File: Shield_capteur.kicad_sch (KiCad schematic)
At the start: 4 parts, among them J1 Power, J2 Digital/PWM, J3 Analog, J4 Digital/PWM

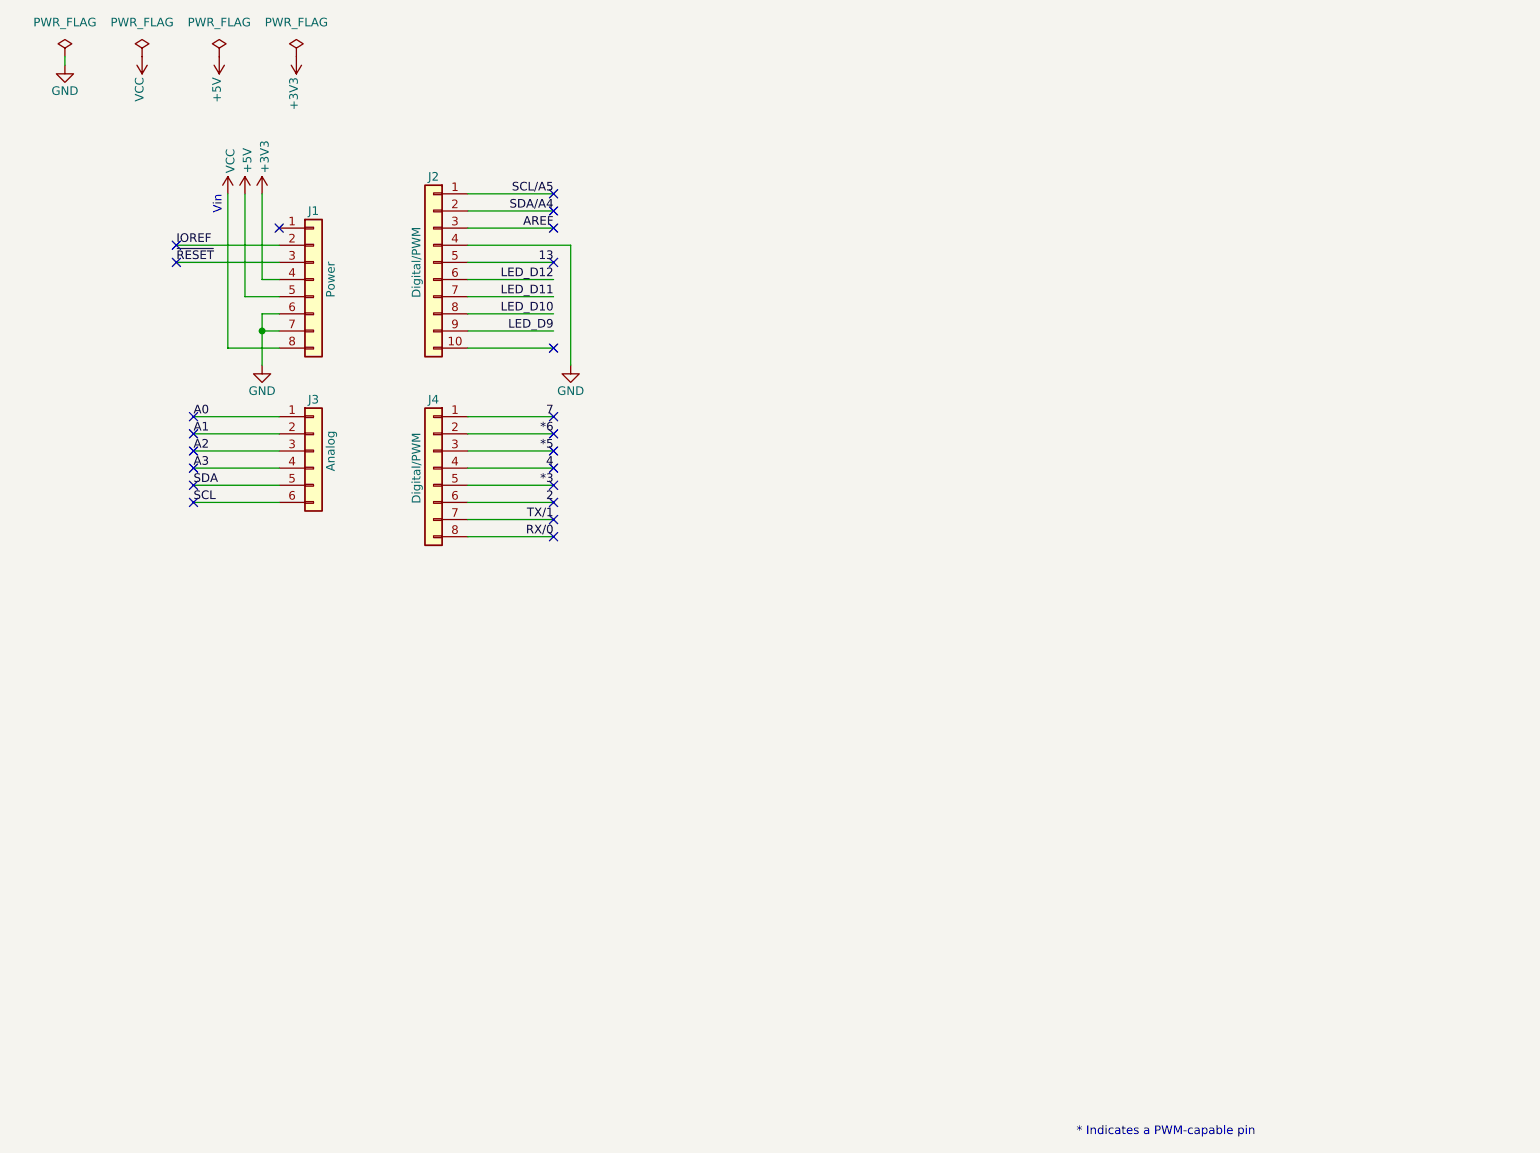
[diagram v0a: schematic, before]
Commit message: Avancée sur le shield, schéma +footprint
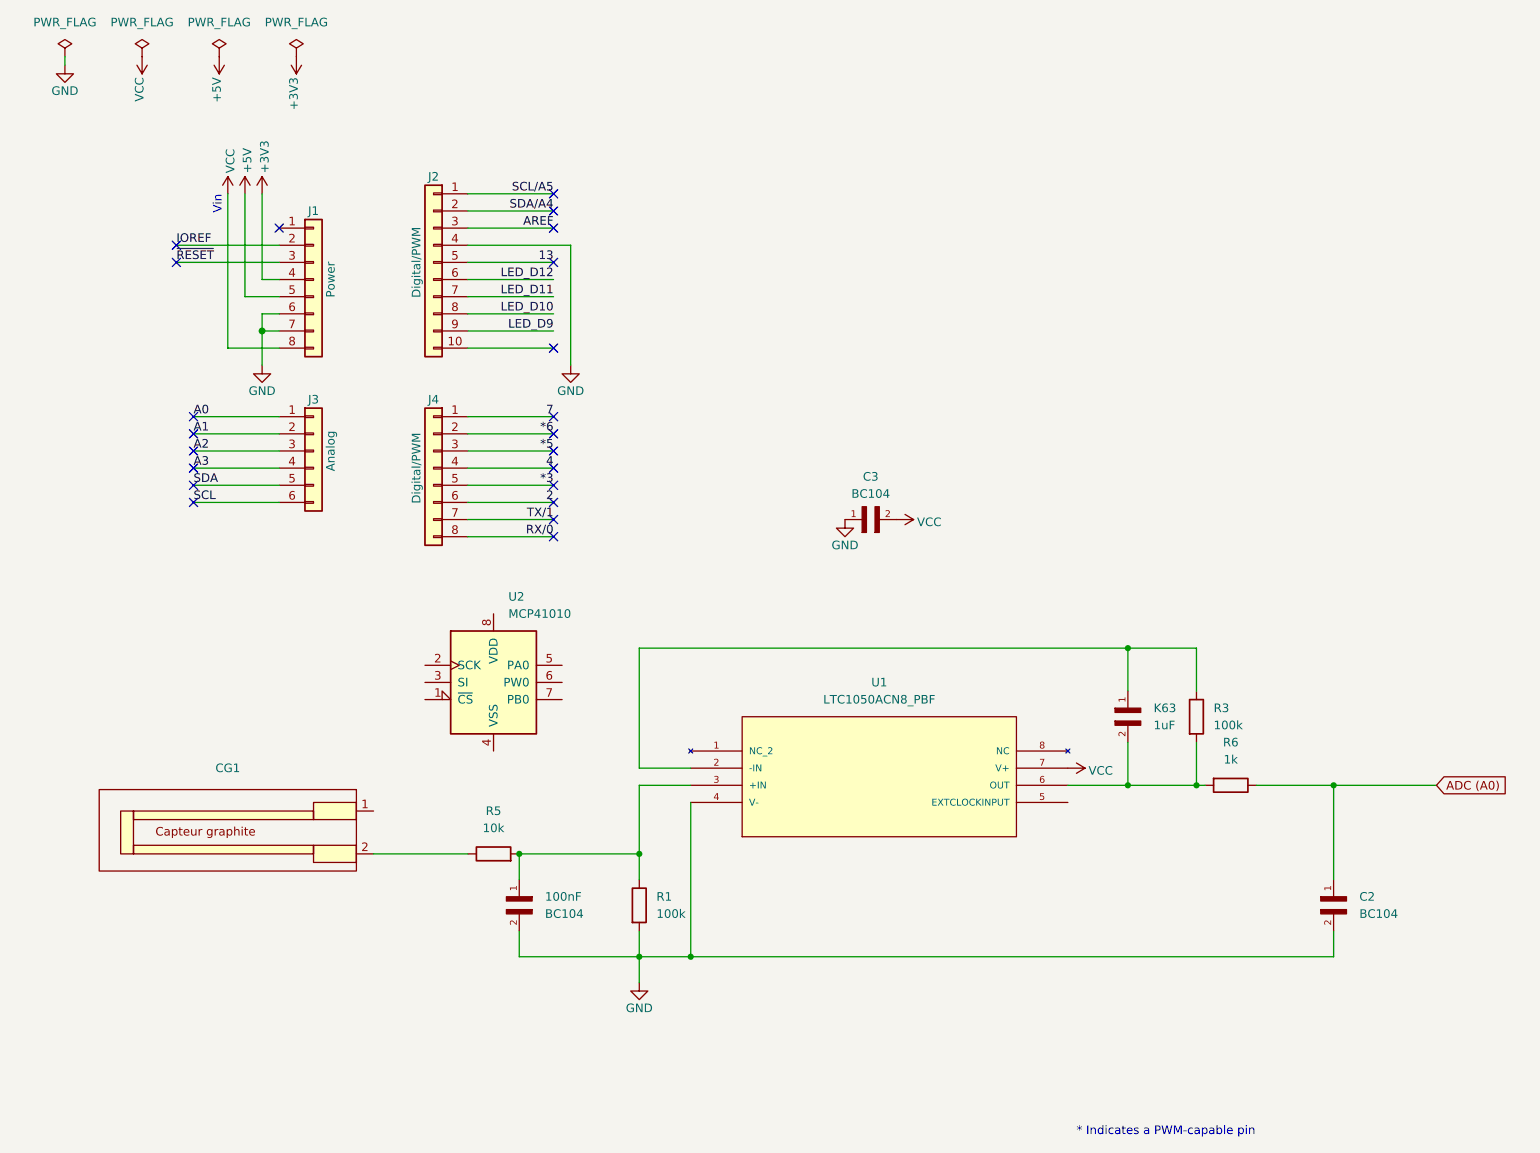
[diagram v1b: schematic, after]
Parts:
- added BC104: 100nF, Capacitor_THT:C_Disc_D5.0mm_W2.5mm_P5.00mm, symbol GRM033B31A104KE84D:GRM033B31A104KE84D
- added C2, C3: BC104, Capacitor_THT:C_Disc_D5.0mm_W2.5mm_P5.00mm, symbol GRM033B31A104KE84D:GRM033B31A104KE84D
- added CG1: ~, Connector_PinSocket_2.54mm:PinSocket_1x02_P2.54mm_Vertical, symbol New_Library_symbol_capteur:Capteur_graphite
- added K63: 1uF, Capacitor_THT:C_Rect_L7.0mm_W4.5mm_P5.00mm, symbol GRM033B31A104KE84D:GRM033B31A104KE84D
- added R1, R3: 100k, Resistor_THT:R_Axial_DIN0207_L6.3mm_D2.5mm_P10.16mm_Horizontal, symbol Device:R
- added R5: 10k, Resistor_THT:R_Axial_DIN0207_L6.3mm_D2.5mm_P10.16mm_Horizontal, symbol Device:R
- added R6: 1k, Resistor_THT:R_Axial_DIN0207_L6.3mm_D2.5mm_P10.16mm_Horizontal, symbol Device:R
- added U1: LTC1050ACN8_PBF, LTC1050ACN8_PBF:PDIP-8_N, symbol LTC1050ACN8_PBF:LTC1050ACN8_PBF
- added U2: MCP41010, symbol Potentiometer_Digital:MCP41010
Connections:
- net GND: now also BC104.2, C2.2, C3.1, R1.2, U1.4 (V-)
- net VCC: now also C3.2, U1.7 (V+)
- new net: BC104.1, R1.1, R5.2, U1.3 (+IN)
- new net: K63.2, R3.2, R6.2, U1.6 (OUT)
- new net: K63.1, R3.1, U1.2 (-IN)
- new net: CG1.2, R5.1
- new net ADC (A0): C2.1, R6.1

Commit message: Progrès TD Datasheet
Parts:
- added HC-1: ~, Connector_PinSocket_2.54mm:PinSocket_1x04_P2.54mm_Vertical, symbol New_Library_symbol_capteur:HC-05
- U2: value MCP41010 -> LTC1050ACN8_PBF; footprint (none) -> LTC1050ACN8_PBF:PDIP-8_N
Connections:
- net 13 is gone; now on net D13: J2.5 (Pin_5)
- net ADC (A0) is gone; now on net A0: C2.1, R6.1
- net LED_D10 is gone; now on net D10: J2.8 (Pin_8)
- net LED_D11 is gone; now on net D11: J2.7 (Pin_7)
- net GND: now also U2.4 (VSS), HC-1. (VCC)
- net VCC: now also CG1.1, U2.8 (VDD), HC-1. (VCC)
- net D8: now reaches J2.10 (Pin_10)
- net D8: now also HC-1. (VCC)
- net at K63.1, R3.1, U1.2 (-IN): now also U2.6 (PW0)
- net D10: now reaches U2.1 (~{CS})
- net D13: now reaches U2.2 (SCK)
- net D11: now reaches U2.3 (SI)
- net 7 renamed D7
- net D7: now also HC-1. (VCC)
- net LED_D12 renamed D12
- net LED_D9 renamed D9
- no-connect marks 22 -> 25
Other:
- moved on the sheet: U2

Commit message: Fin de la schematic
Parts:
- added B1: ~, New_bouton:Boutons_x3, symbol New_Library_symbol_capteur:Boutons_x3
- added Flex1: ~, symbol New_Library_symbol_capteur:Flex_sensor
- added U3: ~, symbol New_Library_symbol_capteur:OLED
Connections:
- net A1: now also Flex1.2 (B)
- net D12: now also B1.5 (Pin_A_B3)
- net D7: now also HC-1.3 (TxD); no longer HC-1. (VCC)
- net D8: now also HC-1.4 (RxD); no longer HC-1. (VCC)
- net GND: now also HC-1.2 (GND), B1.2 (Pin_B_B1), B1.4 (Pin_B_B2), B1.6 (Pin_B_B3), U3.1 (GND); no longer HC-1. (VCC)
- net SCL: now also U3.3 (SCL)
- net SDA: now also U3.4 (SDA)
- net VCC: now also HC-1.1 (VCC), Flex1.1 (A), U3.2 (VCC); no longer HC-1. (VCC)
- net 2 renamed D2
- net D2: now also B1.1 (Pin_A_B1)
- net 4 renamed D4
- net D4: now also B1.3 (Pin_A_B2)
- no-connect marks 25 -> 17
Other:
- moved on the sheet: C3

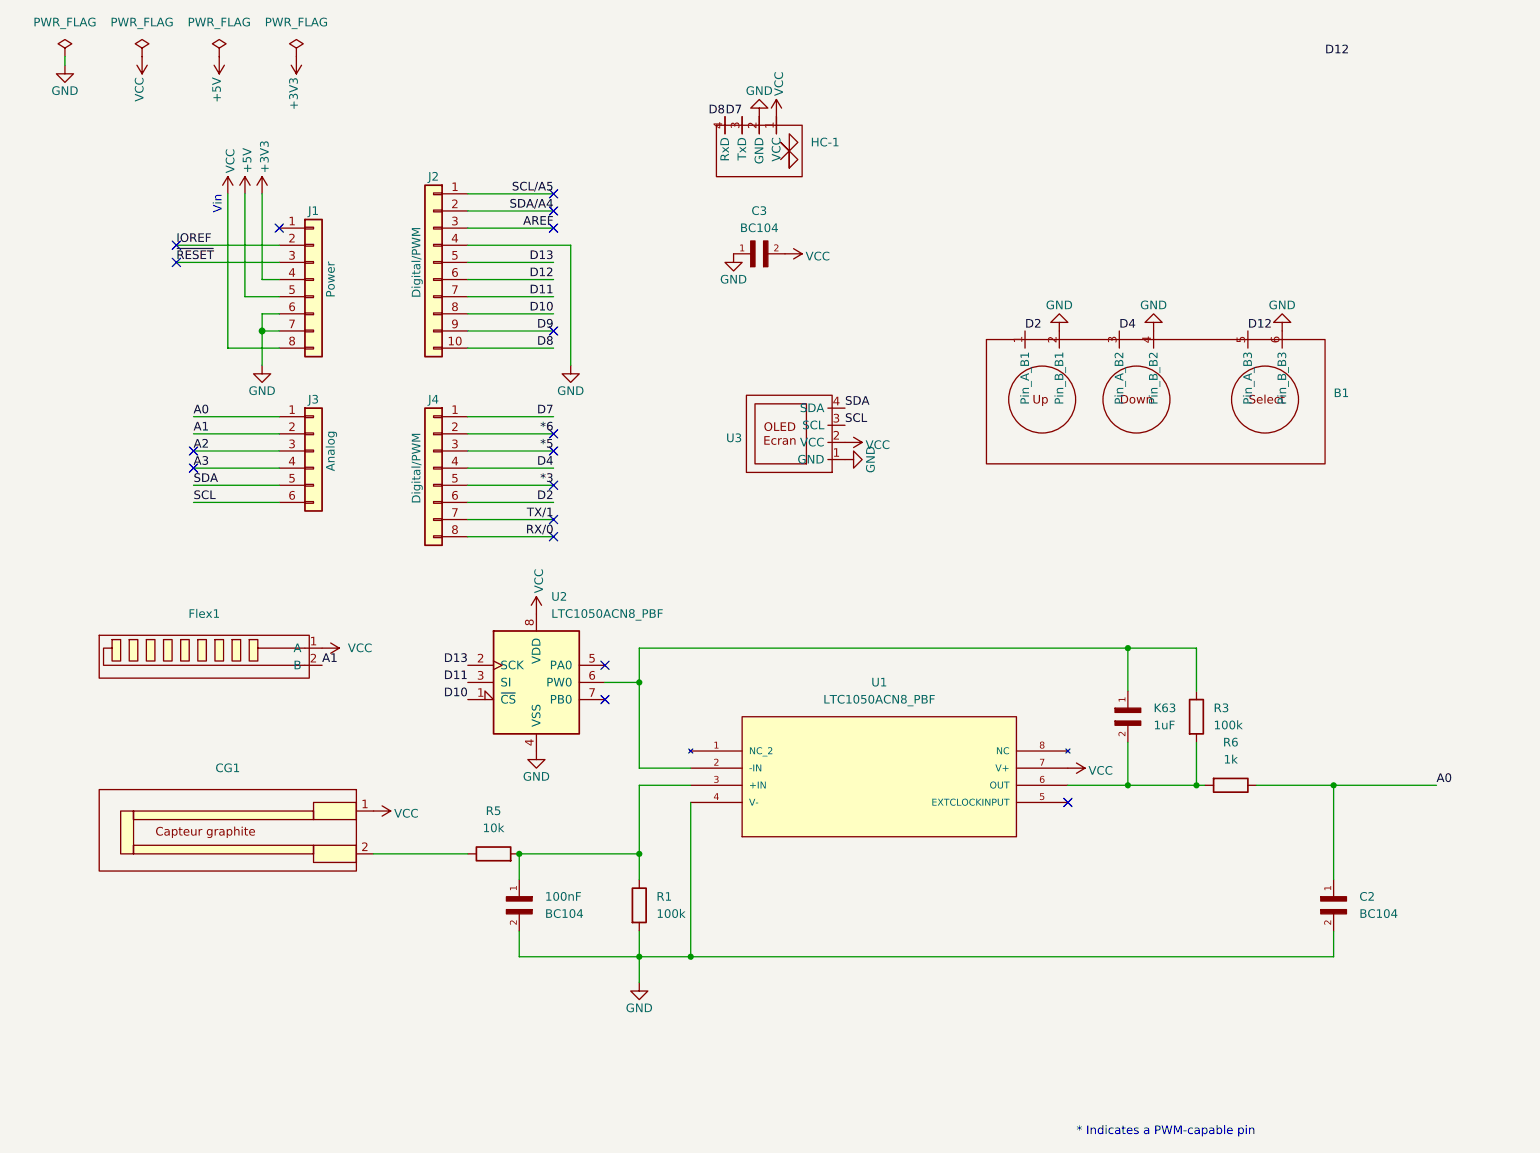
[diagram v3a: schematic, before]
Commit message: Avancé PCB positionnement de tous les composants
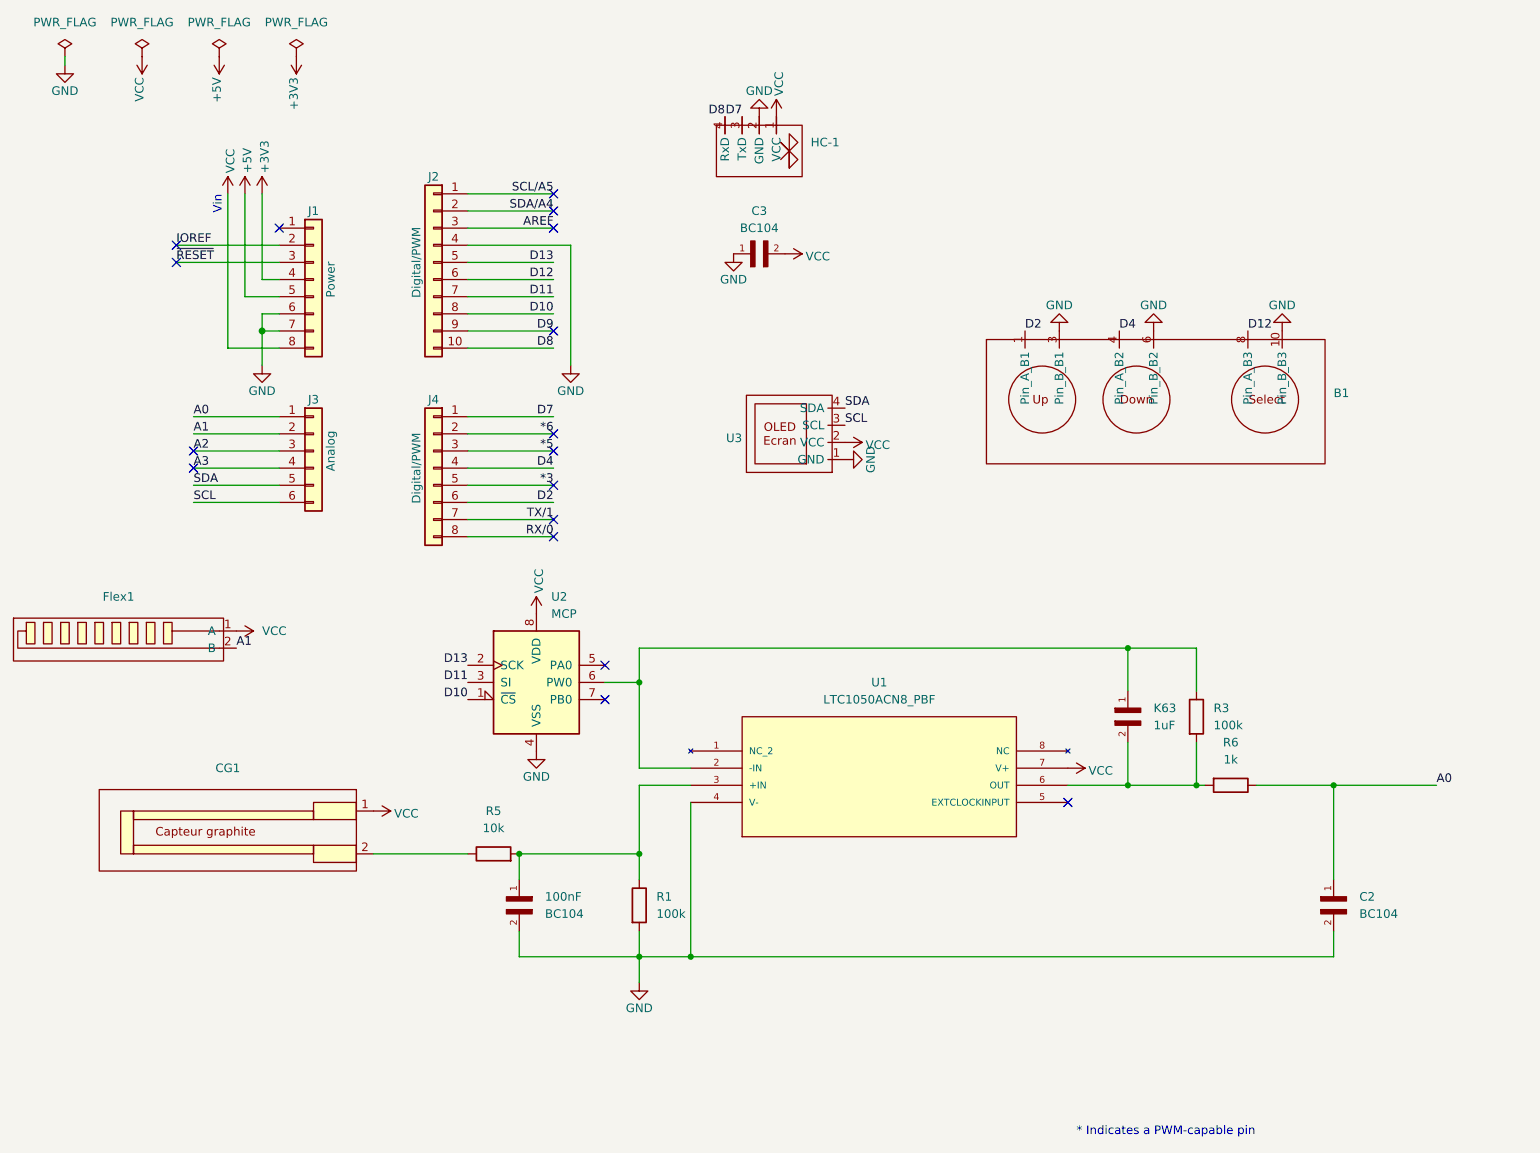
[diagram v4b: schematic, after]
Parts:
- Flex1: footprint (none) -> Connector_PinSocket_2.54mm:PinSocket_1x02_P2.54mm_Vertical
- U2: value LTC1050ACN8_PBF -> MCP
- U3: footprint (none) -> Connector_PinSocket_2.54mm:PinSocket_1x04_P2.54mm_Vertical
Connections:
- net D12: now also B1.8 (Pin_A_B3); no longer B1.5 (Pin_A_B3)
- net D4: now also B1.4 (Pin_A_B2); no longer B1.3 (Pin_A_B2)
- net GND: now also B1.10 (Pin_B_B3), B1.3 (Pin_B_B1); no longer B1.2 (Pin_B_B1), B1.4 (Pin_B_B2)
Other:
- moved on the sheet: Flex1
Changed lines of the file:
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@@
 	)
 	(label "A1"
-		(at 66.04 110.49 0)
+		(at 53.34 107.95 0)
 		(fields_autoplaced yes)
 		(effects
@@
 		)
 	)
-	(label "D12"
-		(at 214.63 20.32 0)
-		(fields_autoplaced yes)
-		(effects
-			(font
-				(size 1.27 1.27)
-			)
-			(justify left bottom)
-		)
-	)
 	(label "A0"
 		(at 46.99 73.66 0)
@@
 			)
 		)
-		(property "Footprint" ""
+		(property "Footprint" "Connector_PinSocket_2.54mm:PinSocket_1x04_P2.54mm_Vertical"
 			(at 135.89 77.47 0)
 			(effects
@@
 	(symbol
 		(lib_id "New_Library_symbol_capteur:Flex_sensor")
-		(at 58.42 109.22 0)
+		(at 45.72 106.68 0)
 		(unit 1)
 		(exclude_from_sim no)
@@
 		(fields_autoplaced yes)
 		(property "Reference" "Flex1"
-			(at 48.5775 102.87 0)
+			(at 35.8775 100.33 0)
 			(effects
 				(font
@@
 		)
 		(property "Value" "~"
-			(at 48.5775 104.14 0)
-			(effects
-				(font
-					(size 1.27 1.27)
-				)
-			)
-		)
-		(property "Footprint" ""
-			(at 58.42 109.22 0)
+			(at 35.8775 101.6 0)
+			(effects
+				(font
+					(size 1.27 1.27)
+				)
+			)
+		)
+		(property "Footprint" "Connector_PinSocket_2.54mm:PinSocket_1x02_P2.54mm_Vertical"
+			(at 45.72 106.68 0)
 			(effects
 				(font
@@
 		)
 		(property "Datasheet" ""
-			(at 58.42 109.22 0)
+			(at 45.72 106.68 0)
 			(effects
 				(font
@@
 		)
 		(property "Description" ""
-			(at 58.42 109.22 0)
+			(at 45.72 106.68 0)
 			(effects
 				(font
@@
 			)
 		)
-		(pin "5"
+		(pin "10"
 		)
 		(pin "4"
@@
 		(pin "6"
 		)
-		(pin "2"
+		(pin "8"
 		)
 		(pin "3"
@@
 	(symbol
 		(lib_id "power:VCC")
-		(at 66.04 107.95 270)
+		(at 53.34 105.41 270)
 		(unit 1)
 		(exclude_from_sim no)
@@
 		(fields_autoplaced yes)
 		(property "Reference" "#PWR021"
-			(at 62.23 107.95 0)
+			(at 49.53 105.41 0)
 			(effects
 				(font
@@
 		)
 		(property "Value" "VCC"
-			(at 69.85 107.9499 90)
+			(at 57.15 105.4099 90)
 			(effects
 				(font
@@
 		)
 		(property "Footprint" ""
-			(at 66.04 107.95 0)
+			(at 53.34 105.41 0)
 			(effects
 				(font
@@
 		)
 		(property "Datasheet" ""
-			(at 66.04 107.95 0)
+			(at 53.34 105.41 0)
 			(effects
 				(font
@@
 		)
 		(property "Description" "Power symbol creates a global label with name \"VCC\""
-			(at 66.04 107.95 0)
+			(at 53.34 105.41 0)
 			(effects
 				(font
@@
 			)
 		)
-		(property "Value" "LTC1050ACN8_PBF"
+		(property "Value" "MCP"
 			(at 99.9841 102.87 0)
 			(effects
